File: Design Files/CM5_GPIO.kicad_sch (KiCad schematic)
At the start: 22 parts, among them J14 Micro_SD_Card_Det, J5 Conn_01x04_MountingPin, J7 Conn_01x04_MountingPin, J8 Conn_01x04_MountingPin, U1 RT9742GGJ5, U21 MCP25625x-x-ML, Y1 Crystal_GND24_Small

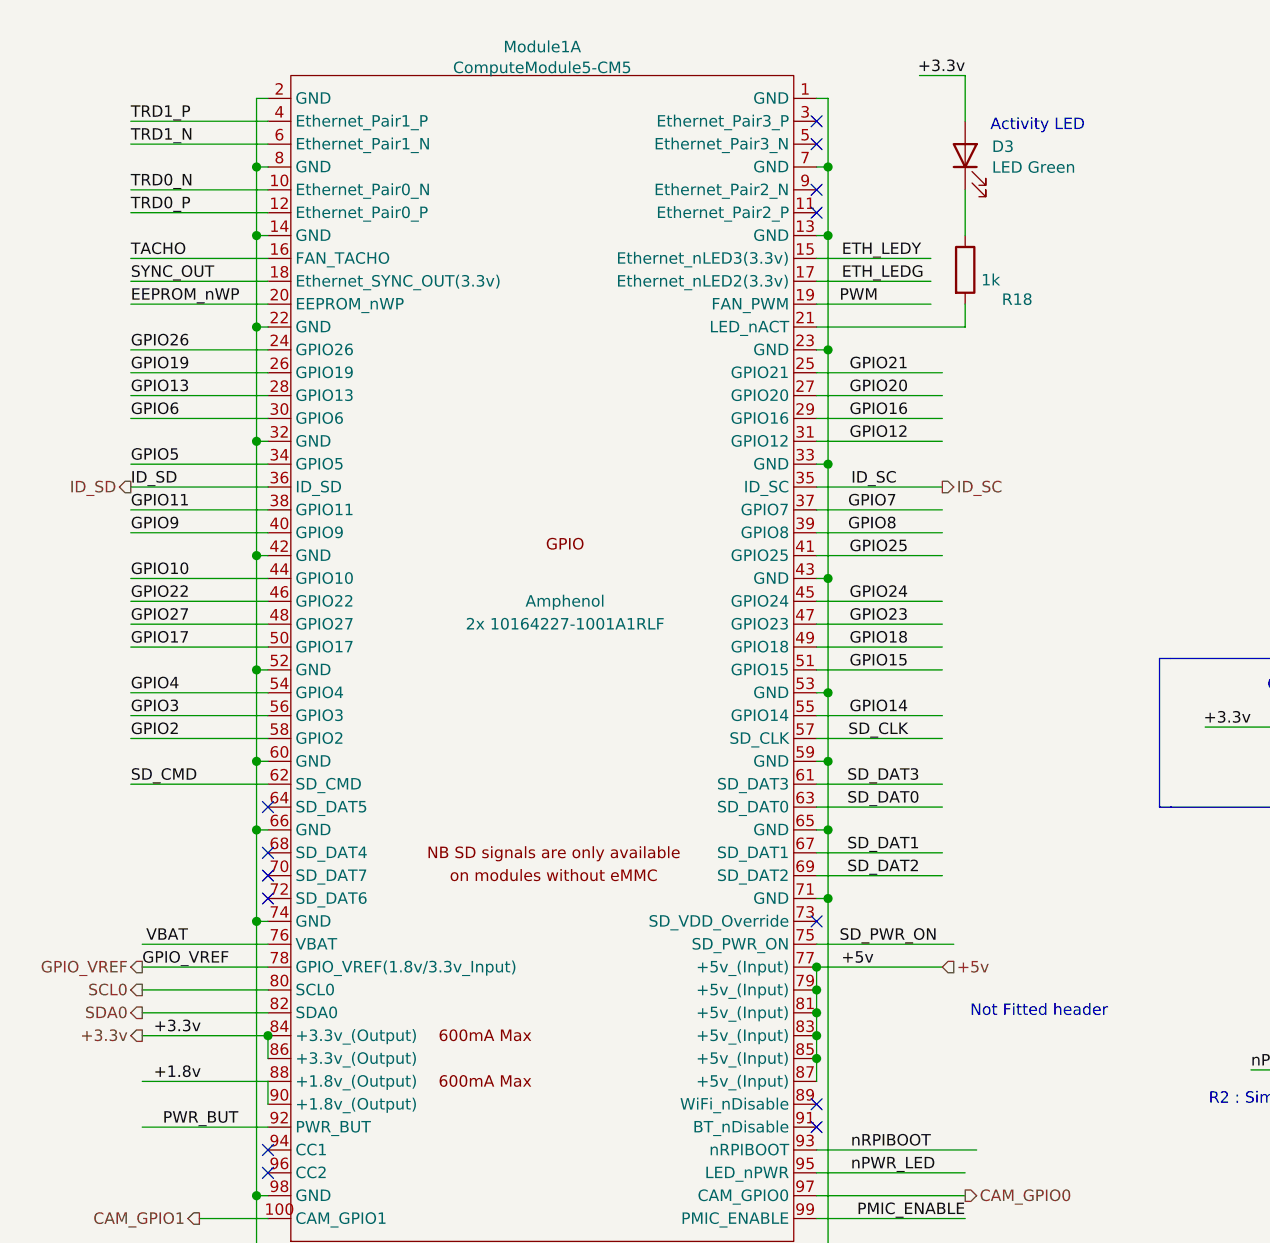
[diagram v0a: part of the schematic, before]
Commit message: Prelim work on autopilot sensors complete
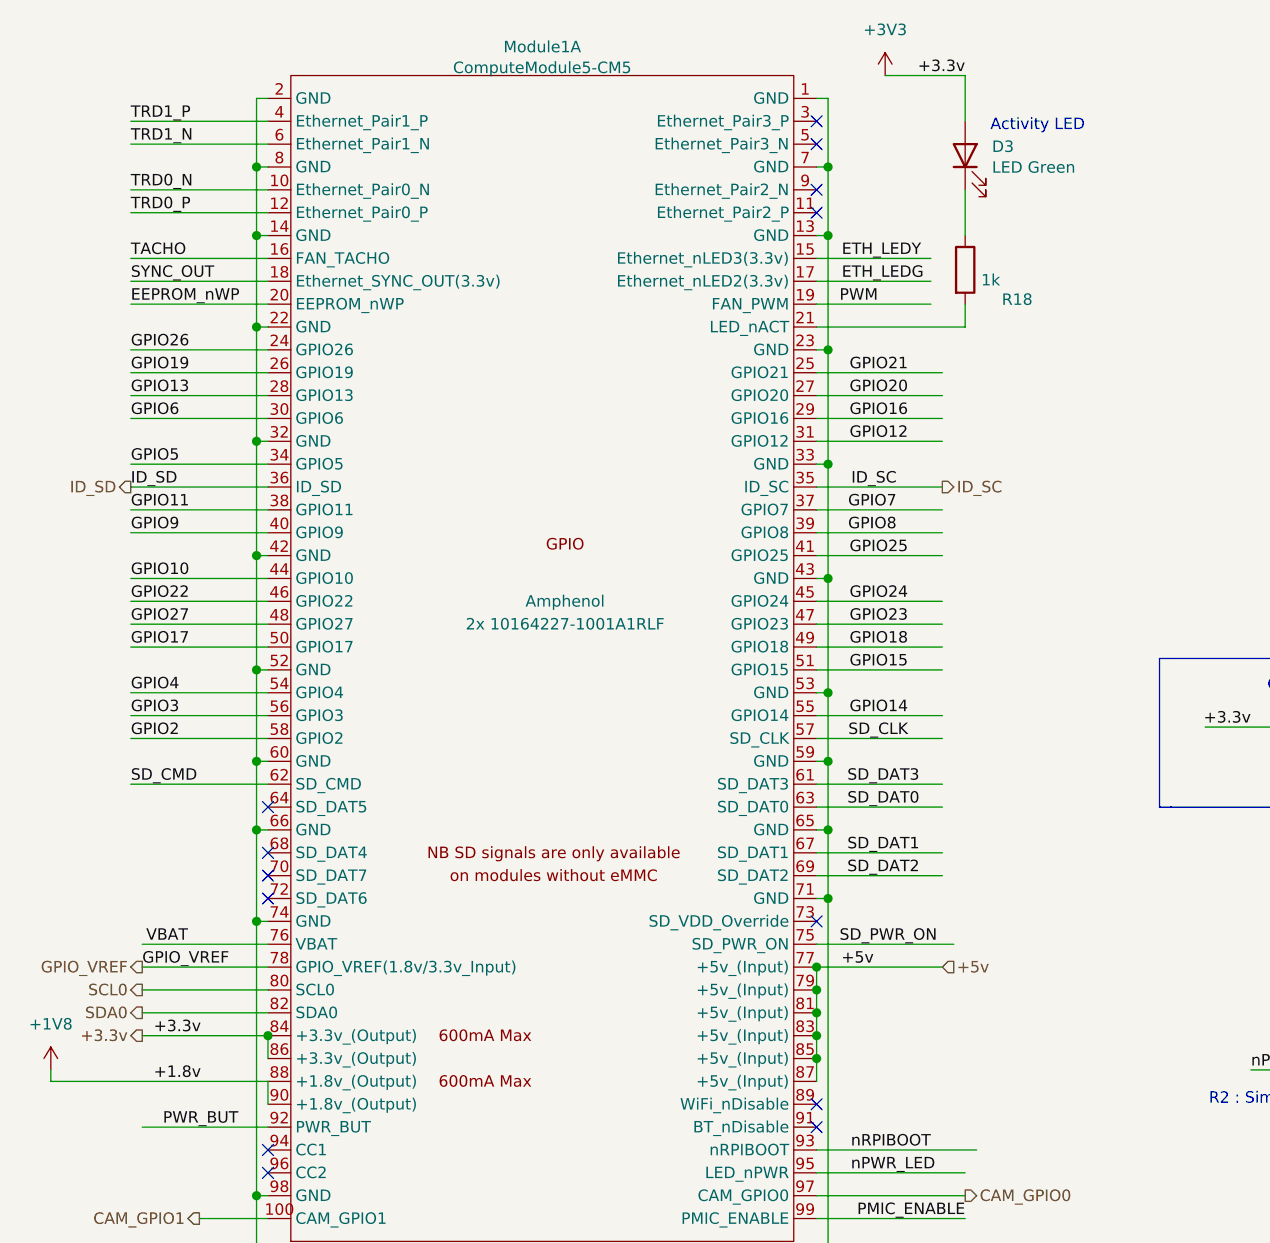
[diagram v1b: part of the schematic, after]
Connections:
- net +1.8v renamed +1V8
- net +3.3v renamed +3V3
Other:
- note removed: "Not Fitted header"
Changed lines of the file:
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@@
 		)
 	)
-	(text "Not Fitted header"
-		(exclude_from_sim no)
-		(at 132.715 123.825 0)
-		(effects
-			(font
-				(size 1.27 1.27)
-			)
-			(justify right bottom)
-		)
-	)
 	(text "Force RPIBOOT = Jumper Pins 1-2 \n"
 		(exclude_from_sim no)
@@
 	(wire
 		(pts
+			(xy 15.24 130.81) (xy 39.37 130.81)
+		)
+		(stroke
+			(width 0)
+			(type default)
+		)
+	)
+	(wire
+		(pts
 			(xy 218.44 123.19) (xy 218.44 118.11)
 		)
@@
 	(wire
 		(pts
-			(xy 100.33 52.07) (xy 114.3 52.07)
+			(xy 15.24 129.54) (xy 15.24 130.81)
 		)
 		(stroke
 			(width 0)
-			(type solid)
+			(type default)
 		)
 	)
 	(wire
 		(pts
-			(xy 227.33 252.73) (xy 222.25 252.73)
+			(xy 100.33 52.07) (xy 114.3 52.07)
 		)
 		(stroke
 			(width 0)
-			(type default)
+			(type solid)
 		)
 	)
 	(wire
 		(pts
-			(xy 25.4 130.81) (xy 39.37 130.81)
+			(xy 227.33 252.73) (xy 222.25 252.73)
 		)
 		(stroke
 			(width 0)
-			(type solid)
+			(type default)
 		)
 	)
@@
 	(wire
 		(pts
+			(xy 107.95 19.05) (xy 116.84 19.05)
+		)
+		(stroke
+			(width 0)
+			(type solid)
+		)
+	)
+	(wire
+		(pts
 			(xy 247.65 210.82) (xy 247.65 208.28)
 		)
@@
 	(wire
 		(pts
-			(xy 111.76 19.05) (xy 116.84 19.05)
-		)
-		(stroke
-			(width 0)
-			(type solid)
-		)
-	)
-	(wire
-		(pts
 			(xy 210.82 128.27) (xy 210.82 129.54)
 		)
@@
 	)
 	(symbol
+		(lib_id "power:+3V3")
+		(at 107.95 19.05 0)
+		(unit 1)
+		(exclude_from_sim no)
+		(in_bom yes)
+		(on_board yes)
+		(dnp no)
+		(fields_autoplaced yes)
+		(property "Reference" "#PWR060"
+			(at 107.95 22.86 0)
+			(effects
+				(font
+					(size 1.27 1.27)
+				)
+				(hide yes)
+			)
+		)
+		(property "Value" "+3V3"
+			(at 107.95 13.97 0)
+			(effects
+				(font
+					(size 1.27 1.27)
+				)
+			)
+		)
+		(property "Footprint" ""
+			(at 107.95 19.05 0)
+			(effects
+				(font
+					(size 1.27 1.27)
+				)
+				(hide yes)
+			)
+		)
+		(property "Datasheet" ""
+			(at 107.95 19.05 0)
+			(effects
+				(font
+					(size 1.27 1.27)
+				)
+				(hide yes)
+			)
+		)
+		(property "Description" "Power symbol creates a global label with name \"+3V3\""
+			(at 107.95 19.05 0)
+			(effects
+				(font
+					(size 1.27 1.27)
+				)
+				(hide yes)
+			)
+		)
+		(pin "1"
+		)
+		(instances
+			(project "compactPi"
+				(path "/e63e39d7-6ac0-4ffd-8aa3-1841a4541b55/00000000-0000-0000-0000-00005cff706a"
+					(reference "#PWR060")
+					(unit 1)
+				)
+			)
+		)
+	)
+	(symbol
 		(lib_id "power:GND")
 		(at 269.24 215.9 0)
@@
 					(unit 1)
 				)
+			)
+		)
+	)
+	(symbol
+		(lib_id "power:+1V8")
+		(at 15.24 129.54 0)
+		(unit 1)
+		(exclude_from_sim no)
+		(in_bom yes)
+		(on_board yes)
+		(dnp no)
+		(fields_autoplaced yes)
+		(property "Reference" "#PWR059"
+			(at 15.24 133.35 0)
+			(effects
+				(font
+					(size 1.27 1.27)
+				)
+				(hide yes)
+			)
+		)
+		(property "Value" "+1V8"
+			(at 15.24 124.46 0)
+			(effects
+				(font
+					(size 1.27 1.27)
+				)
+			)
+		)
+		(property "Footprint" ""
+			(at 15.24 129.54 0)
+			(effects
+				(font
+					(size 1.27 1.27)
+				)
+				(hide yes)
+			)
+		)
+		(property "Datasheet" ""
+			(at 15.24 129.54 0)
+			(effects
+				(font
+					(size 1.27 1.27)
+				)
+				(hide yes)
+			)
+		)
+		(property "Description" "Power symbol creates a global label with name \"+1V8\""
+			(at 15.24 129.54 0)
+			(effects
+				(font
+					(size 1.27 1.27)
+				)
+				(hide yes)
+			)
+		)
+		(pin "1"
+		)
+		(instances
+			(project "compactPi"
+				(path "/e63e39d7-6ac0-4ffd-8aa3-1841a4541b55/00000000-0000-0000-0000-00005cff706a"
+					(reference "#PWR059")
+					(unit 1)
+				)

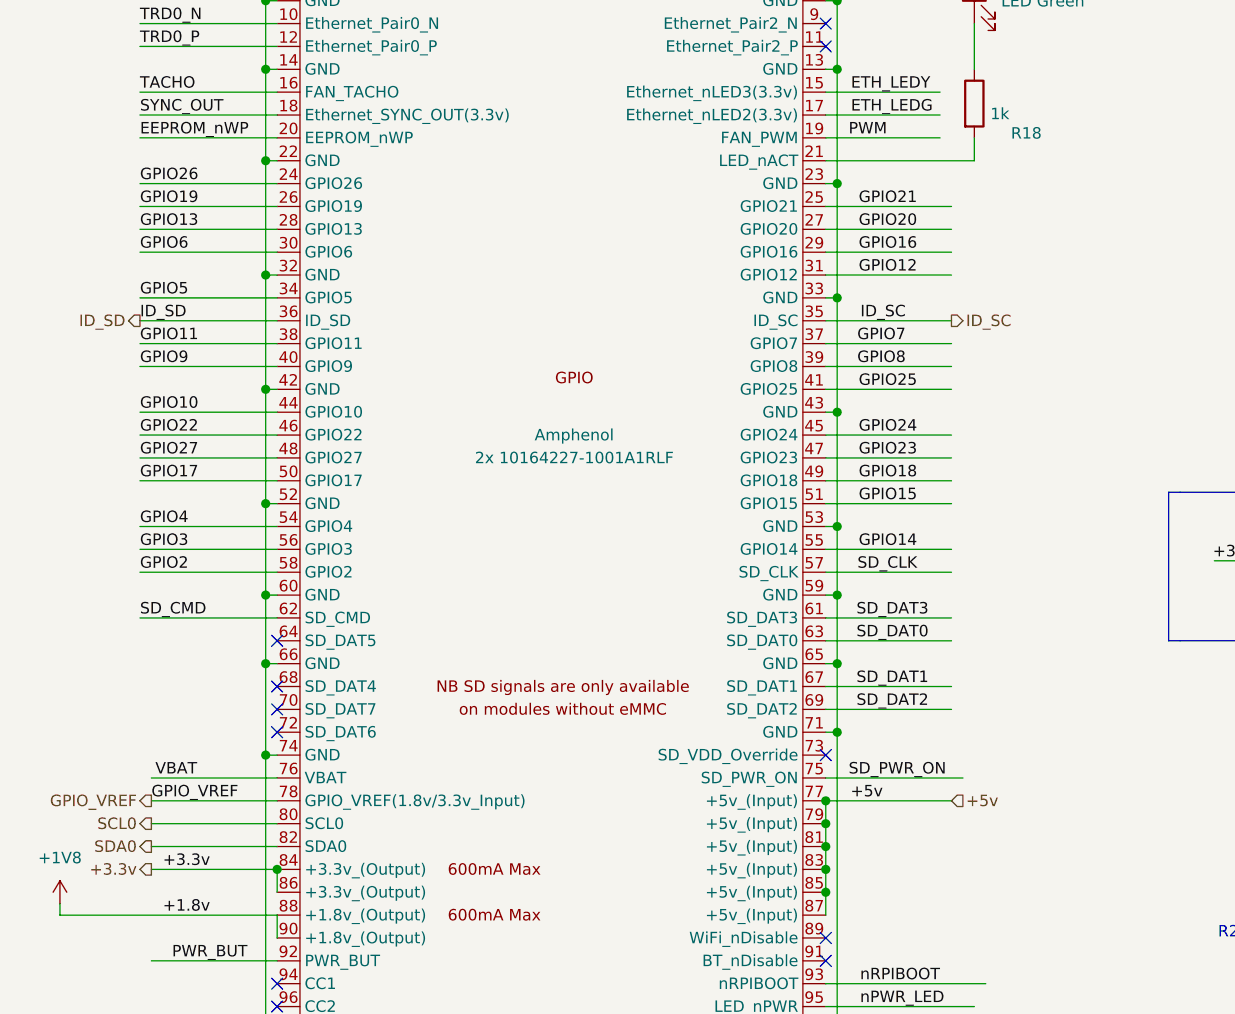
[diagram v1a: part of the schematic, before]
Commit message: Continued adding GPIO interfaces
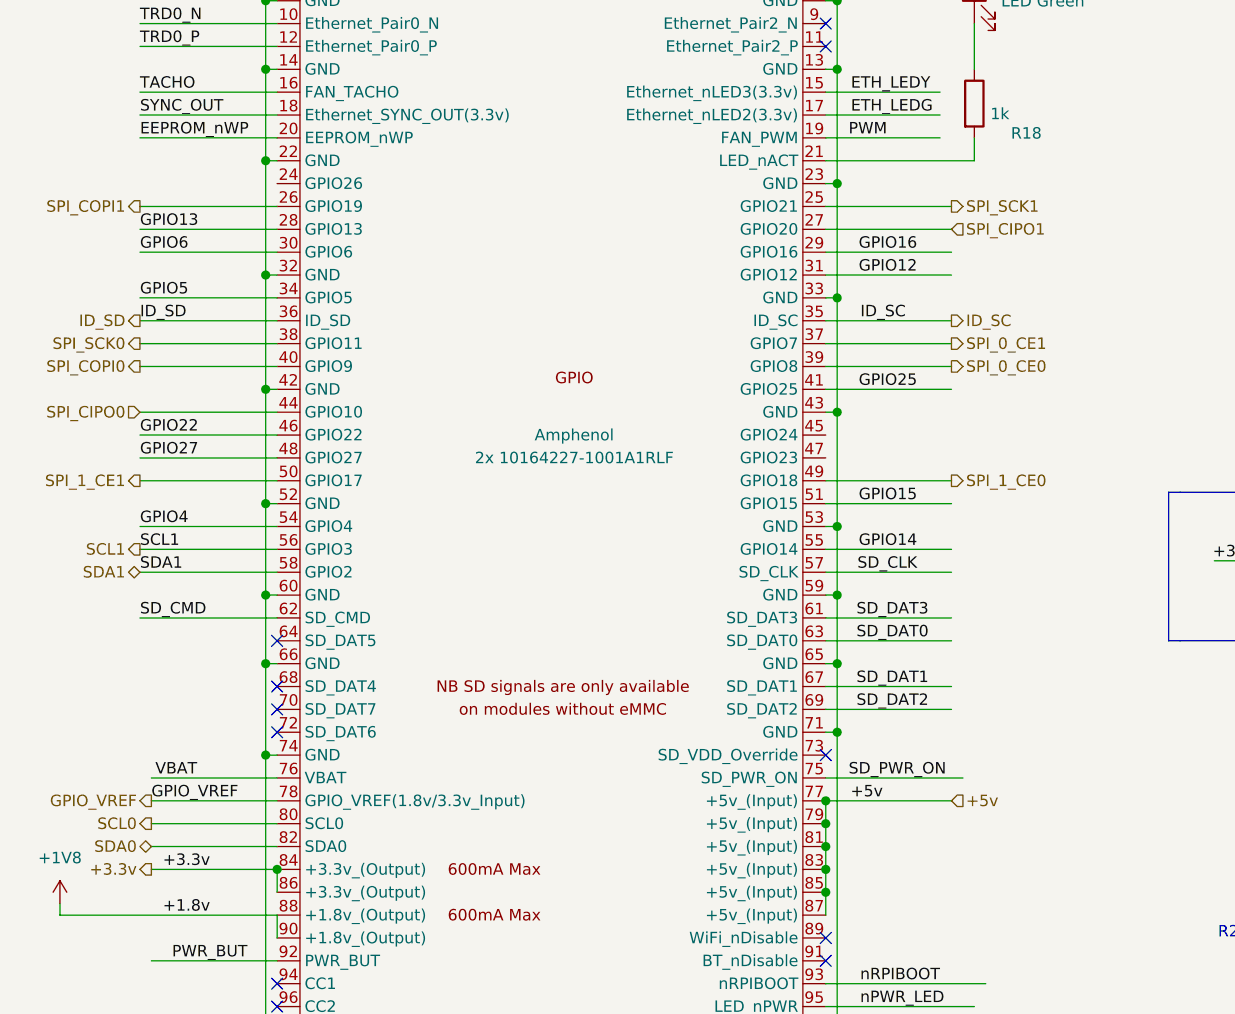
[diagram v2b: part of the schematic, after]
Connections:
- net GPIO10 renamed SPI_CIPO0
- net GPIO11 renamed SPI_SCK0
- net GPIO17 renamed SPI_1_CE1
- net GPIO18 renamed SPI_1_CE0
- net GPIO19 renamed SPI_COPI1
- net GPIO2 renamed SDA1
- net GPIO20 renamed SPI_CIPO1
- net GPIO21 renamed SPI_SCK1
- net GPIO23: no longer names the net of Module1.47 (GPIO23)
- net GPIO24: no longer names the net of Module1.45 (GPIO24)
- net GPIO26: no longer names the net of Module1.24 (GPIO26)
- net GPIO3 renamed SCL1
- net GPIO7 renamed SPI_0_CE1
- net GPIO8 renamed SPI_0_CE0
- net GPIO9 renamed SPI_COPI0

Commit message: More interface interconnects
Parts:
- removed C52, C53: C_Small_US, Capacitor_SMD:C_0402_1005Metric, symbol Device:C_Small_US
- removed J7, J8: Conn_01x04_MountingPin, Connector_JST:JST_GH_BM04B-GHS-TBT_1x04-1MP_P1.25mm_Vertical, symbol Connector_Generic_MountingPin:Conn_01x04_MountingPin
- removed U21: MCP25625x-x-ML, Package_DFN_QFN:QFN-28-1EP_6x6mm_P0.65mm_EP4.25x4.25mm, symbol Interface_CAN_LIN:MCP25625x-x-ML
- removed Y1: Crystal_GND24_Small, Crystal:Crystal_SMD_2016-4Pin_2.0x1.6mm, symbol Device:Crystal_GND24_Small
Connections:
- net +1V8 renamed 1V8_Peripheral
- net +3V3 renamed 3V3_Peripheral
- net +5v renamed 5V0_Core
- no-connect marks 19 -> 17
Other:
- moved on the sheet: C3, C54, C56, D3, D4, J14, J5, Module1A, R18, R19, R20, R21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

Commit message: Fixed power & GPIO nets
Added PWM I2C Bus
Replaced global power labels on the sensor page with hierarchical pins & page labels
Cleaned up CM5 GPIO block sheet
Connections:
- net CAM_GPIO0: no longer names the net of Module1.97 (CAM_GPIO0)
- net CAM_GPIO1: no longer names the net of Module1.100 (CAM_GPIO1)
- net GPIO6 renamed SDA4
- net SPI_0_CE1 renamed SCL4
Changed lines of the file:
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@@
-	(wire
-		(pts
-			(xy 149.86 146.05) (xy 166.37 146.05)
-		)
-		(stroke
-			(width 0)
-			(type solid)
-		)
-	)
 	(wire
 		(pts
@@
 	(wire
 		(pts
+			(xy 149.86 69.85) (xy 163.83 69.85)
+		)
+		(stroke
+			(width 0)
+			(type solid)
+		)
+	)
+	(wire
+		(pts
 			(xy 149.86 110.49) (xy 163.83 110.49)
 		)
@@
 	(wire
 		(pts
-			(xy 81.28 148.59) (xy 88.9 148.59)
-		)
-		(stroke
-			(width 0)
-			(type solid)
-		)
-	)
-	(wire
-		(pts
 			(xy 166.37 21.59) (xy 166.37 26.67)
 		)
@@
 	(wire
 		(pts
+			(xy 73.66 59.69) (xy 88.9 59.69)
+		)
+		(stroke
+			(width 0)
+			(type default)
+		)
+	)
+	(wire
+		(pts
 			(xy 205.74 111.76) (xy 209.55 111.76)
 		)
@@
 	(wire
 		(pts
-			(xy 73.66 59.69) (xy 88.9 59.69)
-		)
-		(stroke
-			(width 0)
-			(type solid)
-		)
-	)
-	(wire
-		(pts
 			(xy 270.51 133.35) (xy 281.94 133.35)
 		)
@@
 		(pts
 			(xy 163.83 95.25) (xy 149.86 95.25)
-		)
-		(stroke
-			(width 0)
-			(type solid)
-		)
-	)
-	(wire
-		(pts
-			(xy 149.86 69.85) (xy 163.83 69.85)
 		)
 		(stroke
@@
 		)
 	)
-	(label "GPIO6"
-		(at 73.66 59.69 0)
-		(effects
-			(font
-				(size 1.27 1.27)
-			)
-			(justify left bottom)
-		)
-	)
 	(label "SD_DAT2"
 		(at 273.05 118.11 0)
@@
 		)
 	)
+	(label "SCL4"
+		(at 163.83 69.85 180)
+		(effects
+			(font
+				(size 1.27 1.27)
+			)
+			(justify right bottom)
+		)
+	)
 	(label "TACHO"
 		(at 73.66 41.91 0)
@@
 	(label "TRD1_RX_P"
 		(at 271.78 53.34 0)
+		(effects
+			(font
+				(size 1.27 1.27)
+			)
+			(justify left bottom)
+		)
+	)
+	(label "SDA4"
+		(at 73.66 59.69 0)
 		(effects
 			(font
@@
 		)
 	)
-	(hierarchical_label "CAM_GPIO1"
-		(shape output)
-		(at 81.28 148.59 180)
-		(effects
-			(font
-				(size 1.27 1.27)
-			)
-			(justify right)
-		)
-	)
 	(hierarchical_label "3V3_Peripheral"
 		(shape output)
@@
 		)
 	)
-	(hierarchical_label "CAM_GPIO0"
-		(shape output)
-		(at 166.37 146.05 0)
-		(effects
-			(font
-				(size 1.27 1.27)
-			)
-			(justify left)
-		)
-	)
-	(hierarchical_label "SPI_0_CE1"
-		(shape output)
-		(at 163.83 69.85 0)
-		(effects
-			(font
-				(size 1.27 1.27)
-			)
-			(justify left)
+	(hierarchical_label "SDA4"
+		(shape bidirectional)
+		(at 73.66 59.69 180)
+		(effects
+			(font
+				(size 1.27 1.27)
+			)
+			(justify right)
 		)
 	)
@@
 		)
 	)
+	(hierarchical_label "SCL4"
+		(shape output)
+		(at 163.83 69.85 0)
+		(effects
+			(font
+				(size 1.27 1.27)
+			)
+			(justify left)
+		)
+	)
